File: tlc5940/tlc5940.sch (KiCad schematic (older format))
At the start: 5 parts, among them P1 DIL28, U2 TLC5940PWP

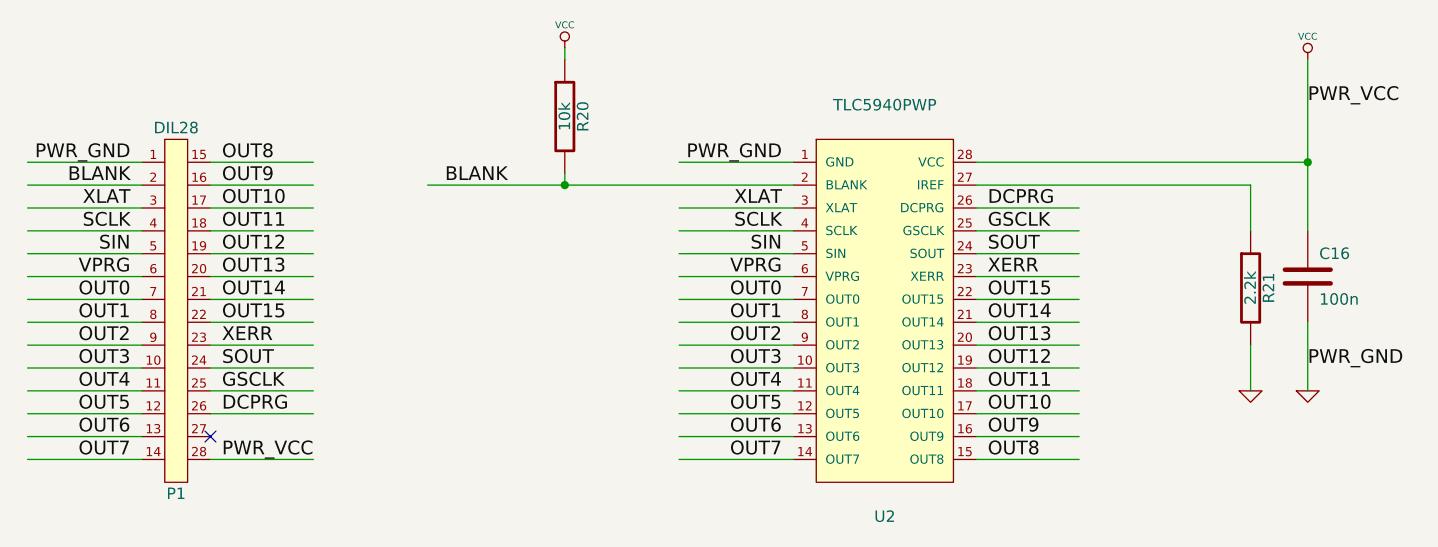
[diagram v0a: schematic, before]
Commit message: break out all pins to make board more generic
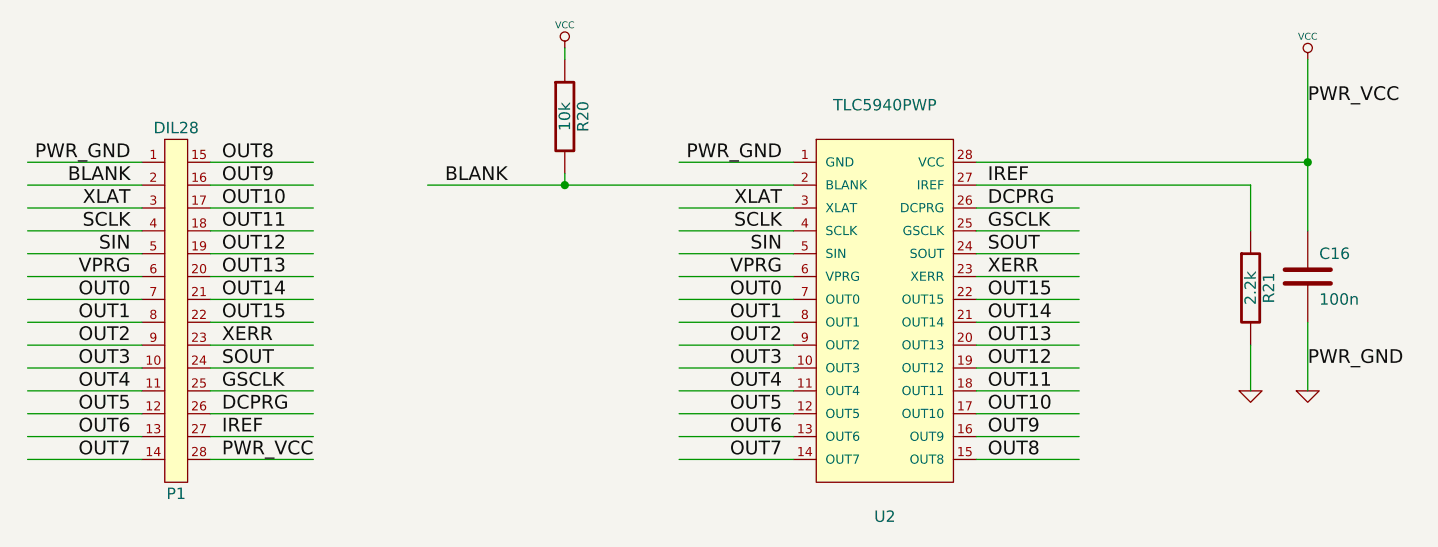
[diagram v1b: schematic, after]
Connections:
- net labels added: IREF
- wire segments 61 -> 62
- no-connect marks 1 -> 0
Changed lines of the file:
@@
-EESchema Schematic File Version 2  date Sun 15 Apr 2012 04:47:11 PM CEST
-LIBS:power
-LIBS:device
-LIBS:transistors
-LIBS:conn
-LIBS:linear
-LIBS:regul
-LIBS:74xx
-LIBS:cmos4000
-LIBS:adc-dac
-LIBS:memory
-LIBS:xilinx
-LIBS:special
-LIBS:microcontrollers
-LIBS:dsp
-LIBS:microchip
-LIBS:analog_switches
-LIBS:motorola
-LIBS:texas
-LIBS:intel
-LIBS:audio
-LIBS:interface
-LIBS:digital-audio
-LIBS:philips
-LIBS:display
-LIBS:cypress
-LIBS:siliconi
-LIBS:opto
-LIBS:atmel
-LIBS:contrib
-LIBS:valves
-LIBS:open-project
+EESchema Schematic File Version 2  date Fri 20 Apr 2012 07:31:05 PM CEST
 LIBS:tlc5940-cache
 EELAYER 25  0
@@
 Sheet 1 1
 Title ""
-Date "15 apr 2012"
+Date "20 apr 2012"
 Rev ""
 Comp "open-project.ch"
@@
 Text Label 2800 2950 0    60   ~ 0
 OUT8
+Text Label 2800 4250 0    60   ~ 0
+PWR_VCC
+Text Label 7550 3850 0    60   ~ 0
+PWR_GND
 Wire Wire Line
 	5300 3150 4800 3150
@@
 Wire Wire Line
 	2750 4250 3200 4250
-Text Label 2800 4250 0    60   ~ 0
-PWR_VCC
-NoConn ~ 2750 4150
-Text Label 7550 3850 0    60   ~ 0
-PWR_GND
+Wire Wire Line
+	2750 4150 3200 4150
+Text Label 6150 3050 0    60   ~ 0
+IREF
+Text Label 2800 4150 0    60   ~ 0
+IREF
 $EndSCHEMATC
